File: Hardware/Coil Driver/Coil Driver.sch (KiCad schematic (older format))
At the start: 88 parts, among them J1 Barrel_Jack_Switch, J2 0.1\" Header, J3 Tag-connect-NL, J4 0.1\" Header, Q1 DMN3023L, Q2 DMN3023L, Q3 DMN3023L, Q4 DMN3023L, SW1 BTN_RST, SW2 BTN_USR1, SW3 BTN_USR2, U1 DGD05473, U2 MCP16331, U3 DGD05473, U4 STM32F070F6P6

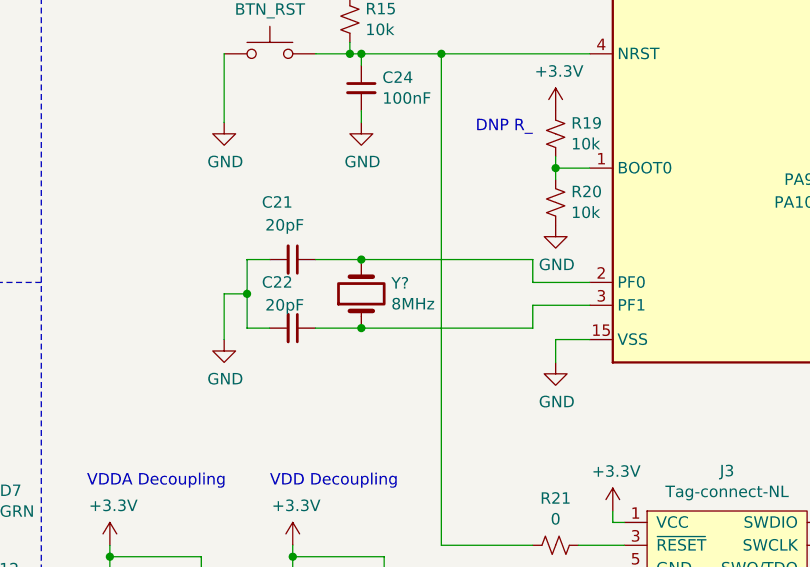
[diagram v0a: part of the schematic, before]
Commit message: completed first draft of part placement, and switching loop layout of gate drivers
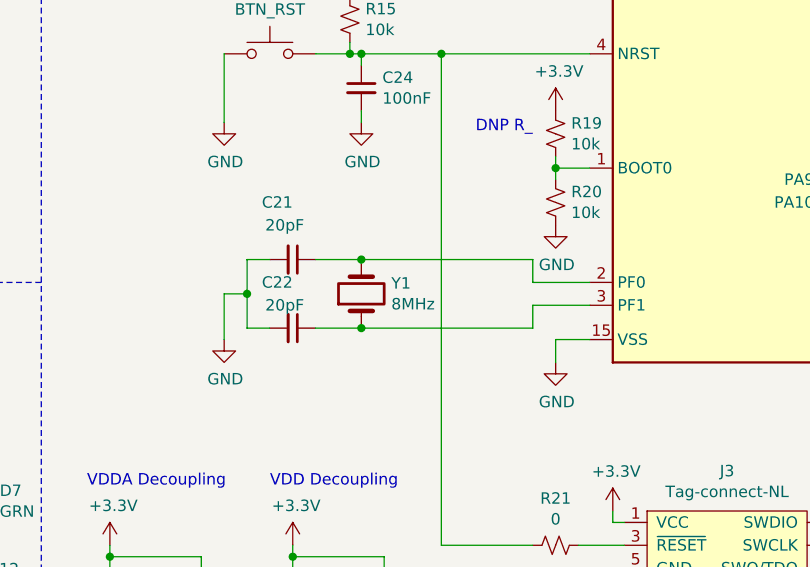
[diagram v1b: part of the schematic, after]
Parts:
- C6, C7, C8: footprint Capacitor_SMD:C_0603_1608Metric -> Capacitor_SMD:C_0402_1005Metric
- R18, R3: footprint Resistor_SMD:R_0603_1608Metric -> Resistor_SMD:R_0805_2012Metric
- Y1: renamed from Y?; footprint (none) -> Crystal:Crystal_SMD_5032-2Pin_5.0x3.2mm
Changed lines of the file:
@@
 F 0 "R3" V 2245 5100 50  0000 C CNN
 F 1 "10" V 2336 5100 50  0000 C CNN
-F 2 "Resistor_SMD:R_0603_1608Metric" H 2450 5100 50  0001 C CNN
+F 2 "Resistor_SMD:R_0805_2012Metric" H 2450 5100 50  0001 C CNN
 F 3 "~" H 2450 5100 50  0001 C CNN
 	1    2450 5100
@@
 F 0 "C8" V 2950 5150 50  0000 R CNN
 F 1 "100nF" V 2850 5200 50  0000 R CNN
-F 2 "Capacitor_SMD:C_0603_1608Metric" H 2750 5100 50  0001 C CNN
+F 2 "Capacitor_SMD:C_0402_1005Metric" H 2750 5100 50  0001 C CNN
 F 3 "~" H 2750 5100 50  0001 C CNN
 	1    2750 5100
@@
 F 0 "R18" V 6845 5100 50  0000 C CNN
 F 1 "10" V 6936 5100 50  0000 C CNN
-F 2 "Resistor_SMD:R_0603_1608Metric" H 7050 5100 50  0001 C CNN
+F 2 "Resistor_SMD:R_0805_2012Metric" H 7050 5100 50  0001 C CNN
 F 3 "~" H 7050 5100 50  0001 C CNN
 	1    7050 5100
@@
 F 0 "C7" H 2792 3246 50  0000 L CNN
 F 1 "100nF" H 2792 3155 50  0000 L CNN
-F 2 "Capacitor_SMD:C_0603_1608Metric" H 2700 3200 50  0001 C CNN
+F 2 "Capacitor_SMD:C_0402_1005Metric" H 2700 3200 50  0001 C CNN
 F 3 "~" H 2700 3200 50  0001 C CNN
 	1    2700 3200
@@
 F 0 "C6" H 2258 7146 50  0000 R CNN
 F 1 "100nF" H 2258 7055 50  0000 R CNN
-F 2 "Capacitor_SMD:C_0603_1608Metric" H 2350 7100 50  0001 C CNN
+F 2 "Capacitor_SMD:C_0402_1005Metric" H 2350 7100 50  0001 C CNN
 F 3 "~" H 2350 7100 50  0001 C CNN
 	1    2350 7100
@@
 	6200 2400 6400 2400
 $Comp
-L Device:Crystal Y?
+L Device:Crystal Y1
 U 1 1 60550A6D
 P 6400 2550
-F 0 "Y?" V 6446 2419 50  0000 R CNN
+F 0 "Y1" V 6446 2419 50  0000 R CNN
 F 1 "8MHz" V 6355 2419 50  0000 R CNN
-F 2 "" H 6400 2550 50  0001 C CNN
+F 2 "Crystal:Crystal_SMD_5032-2Pin_5.0x3.2mm" H 6400 2550 50  0001 C CNN
 F 3 "~" H 6400 2550 50  0001 C CNN
 	1    6400 2550

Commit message: Added internal layers, routed power input and buck converter, and repositioned a few components. Defined PCB shape and moved to center of drawing template.
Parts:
- L2: footprint Connector_PinHeader_2.54mm:PinHeader_1x02_P2.54mm_Vertical -> Connector_PinSocket_2.54mm:PinSocket_1x02_P2.54mm_Vertical
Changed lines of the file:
@@
 F 0 "L2" V 5100 5500 50  0000 C CNN
 F 1 "COIL" V 4950 5500 50  0000 C CNN
-F 2 "Connector_PinHeader_2.54mm:PinHeader_1x02_P2.54mm_Vertical" H 5000 5500 50  0001 C CNN
+F 2 "Connector_PinSocket_2.54mm:PinSocket_1x02_P2.54mm_Vertical" H 5000 5500 50  0001 C CNN
 F 3 "~" H 5000 5500 50  0001 C CNN
 	1    5000 5500

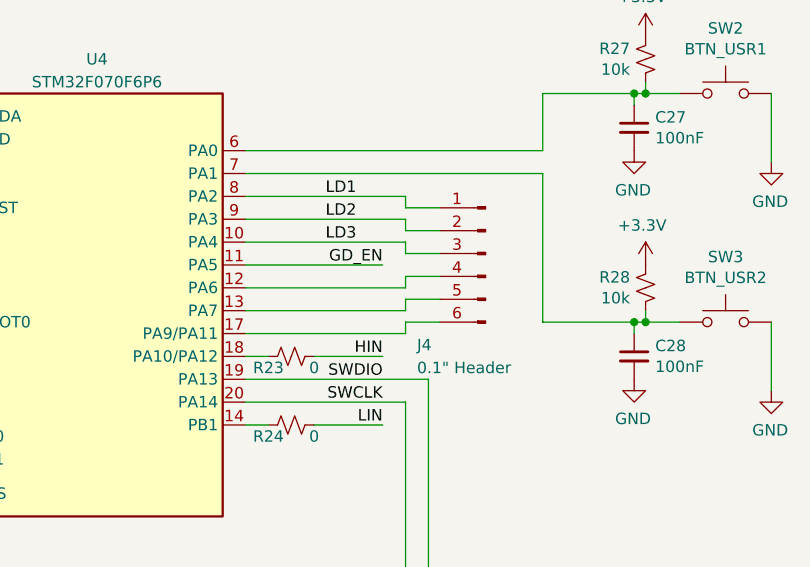
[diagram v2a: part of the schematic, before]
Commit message: Done with initial routing of microcontroller. Flipped order of extra IO exposed on header to ease routing. Added some power pours
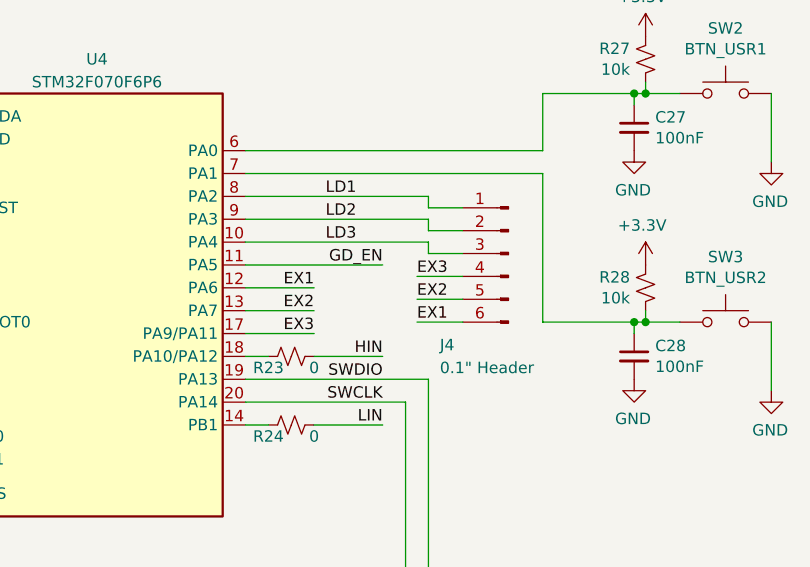
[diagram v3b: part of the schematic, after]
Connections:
- net EX1: now reaches U4.12 (PA6)
- net EX1: now also J4.6 (Pin_6); no longer J4.4 (Pin_4)
- net EX2: now reaches J4.5 (Pin_5), U4.13 (PA7)
- net EX3: now reaches U4.17 (PA9/PA11)
- net EX3: now also J4.4 (Pin_4); no longer J4.6 (Pin_6)
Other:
- moved on the sheet: J4
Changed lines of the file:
@@
 Wire Wire Line
 	10000 1350 10000 2000
-Text Label 9300 1750 2    50   ~ 0
-GD_EN
 Text Label 9300 2150 2    50   ~ 0
 HIN
@@
 L Connector:Conn_01x06_Male J4
 U 1 1 600594E3
-P 9750 1700
-F 0 "J4" H 10050 1300 50  0000 R CNN
-F 1 "0.1\" Header" H 10050 1200 50  0000 R CNN
-F 2 "Connector_PinHeader_2.54mm:PinHeader_1x06_P2.54mm_Vertical" H 9750 1700 50  0001 C CNN
-F 3 "~" H 9750 1700 50  0001 C CNN
-	1    9750 1700
-	-1   0    0    -1
-$EndComp
-Wire Wire Line
-	8700 1450 9400 1450
-Wire Wire Line
-	8700 2050 9400 2050
-Wire Wire Line
-	9400 2050 9400 2000
-Wire Wire Line
-	9400 2000 9550 2000
+P 9850 1700
+F 0 "J4" H 10150 1300 50  0000 R CNN
+F 1 "0.1\" Header" H 10150 1200 50  0000 R CNN
+F 2 "Connector_PinHeader_2.54mm:PinHeader_1x06_P2.54mm_Vertical" H 9850 1700 50  0001 C CNN
+F 3 "~" H 9850 1700 50  0001 C CNN
+	1    9850 1700
+	-1   0    0    -1
+$EndComp
 Wire Wire Line
 	9000 2150 9300 2150
@@
 $EndComp
 Wire Wire Line
-	8700 1950 9400 1950
-Wire Wire Line
-	9400 1950 9400 1900
-Wire Wire Line
-	9400 1900 9550 1900
-Wire Wire Line
-	9400 1850 9400 1800
-Wire Wire Line
-	9400 1800 9550 1800
-Wire Wire Line
-	8700 1850 9400 1850
-Wire Wire Line
-	9400 1650 9400 1700
-Wire Wire Line
-	9400 1700 9550 1700
-Wire Wire Line
-	8700 1650 9400 1650
-Wire Wire Line
-	9400 1550 9400 1600
-Wire Wire Line
-	9400 1600 9550 1600
-Wire Wire Line
-	8700 1550 9400 1550
-Wire Wire Line
-	9400 1450 9400 1500
-Wire Wire Line
-	9400 1500 9550 1500
+	9500 1650 9500 1700
+Wire Wire Line
+	9500 1700 9650 1700
+Wire Wire Line
+	9500 1550 9500 1600
+Wire Wire Line
+	9500 1600 9650 1600
+Wire Wire Line
+	9500 1450 9500 1500
+Wire Wire Line
+	9500 1500 9650 1500
 $Comp
 L Device:C_Small C20
@@
 	0    1    1    0
 $EndComp
-Text Label 9050 1450 0    50   ~ 0
-LD1
-Text Label 9050 1550 0    50   ~ 0
-LD2
-Text Label 9050 1650 0    50   ~ 0
-LD3
 $Comp
 L Device:LED D10
@@
 Wire Wire Line
 	6400 2400 7150 2400
+Wire Wire Line
+	8700 1850 9000 1850
+Wire Wire Line
+	8700 1950 9000 1950
+Wire Wire Line
+	8700 2050 9000 2050
+Text Label 9000 1850 2    50   ~ 0
+EX1
+Text Label 9000 1950 2    50   ~ 0
+EX2
+Text Label 9000 2050 2    50   ~ 0
+EX3
+Text Label 9450 2000 0    50   ~ 0
+EX1
+Text Label 9450 1900 0    50   ~ 0
+EX2
+Text Label 9450 1800 0    50   ~ 0
+EX3
+Wire Wire Line
+	9650 1800 9450 1800
+Wire Wire Line
+	9450 1900 9650 1900
+Wire Wire Line
+	9650 2000 9450 2000
+Wire Wire Line
+	8700 1450 9500 1450
+Wire Wire Line
+	8700 1550 9500 1550
+Wire Wire Line
+	8700 1650 9500 1650
+Text Label 9300 1750 2    50   ~ 0
+GD_EN
+Text Label 9050 1650 0    50   ~ 0
+LD3
+Text Label 9050 1550 0    50   ~ 0
+LD2
+Text Label 9050 1450 0    50   ~ 0
+LD1
 $EndSCHEMATC

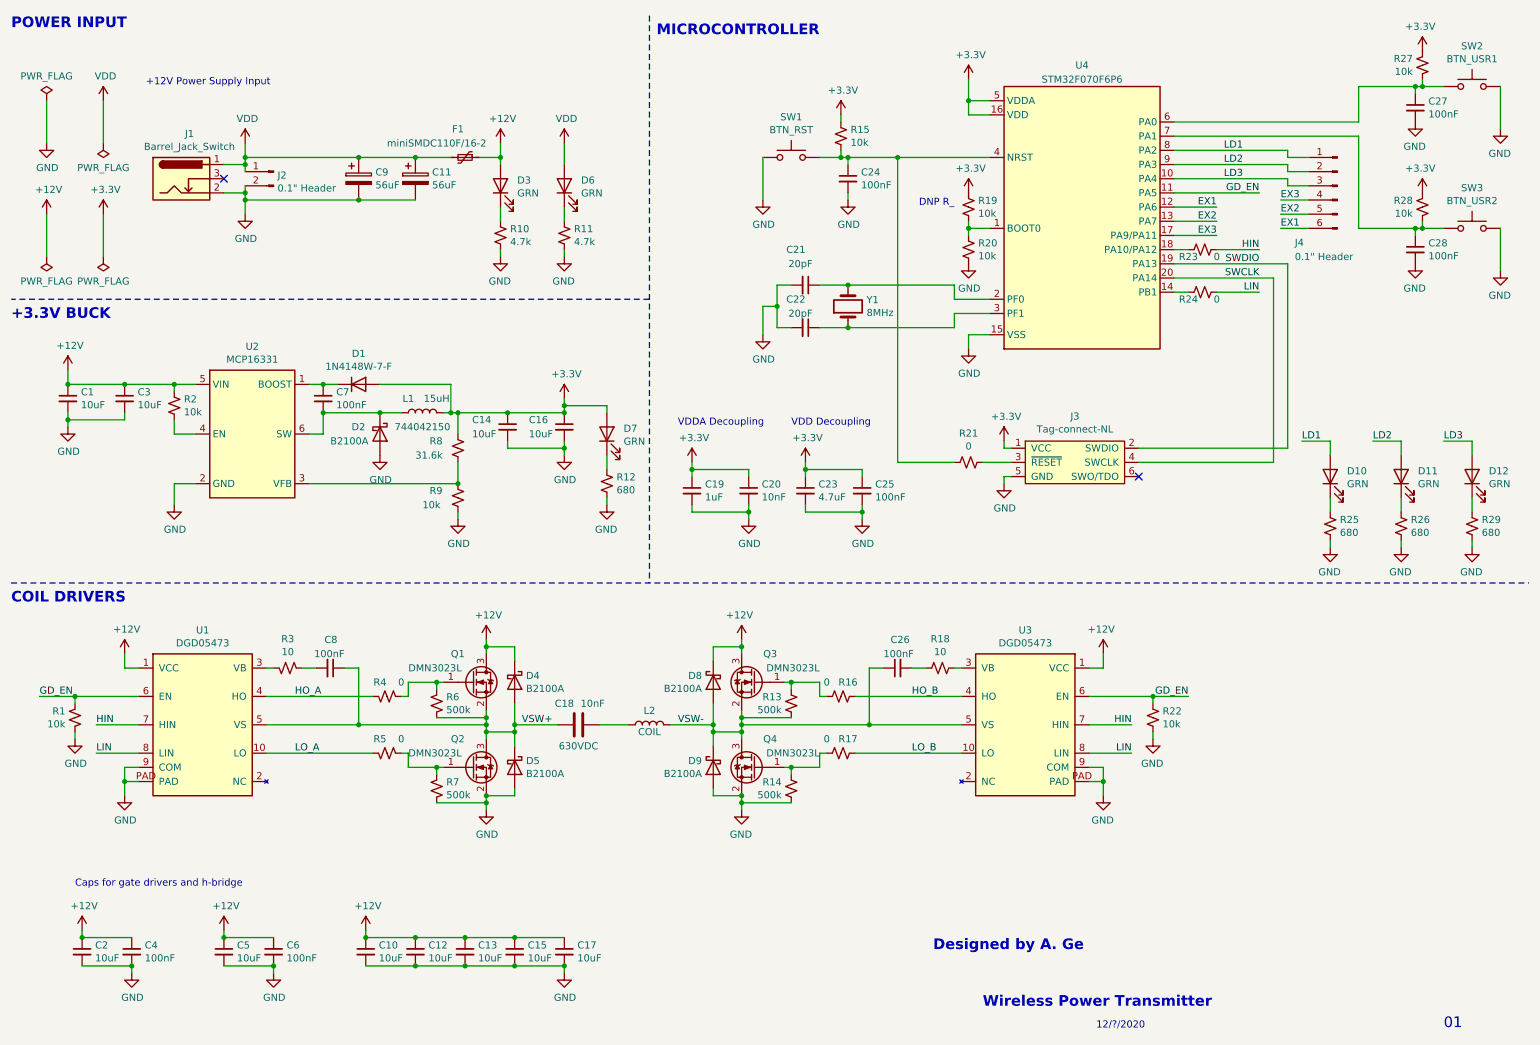
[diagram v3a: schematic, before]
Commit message: Positioned all designators and added logo library
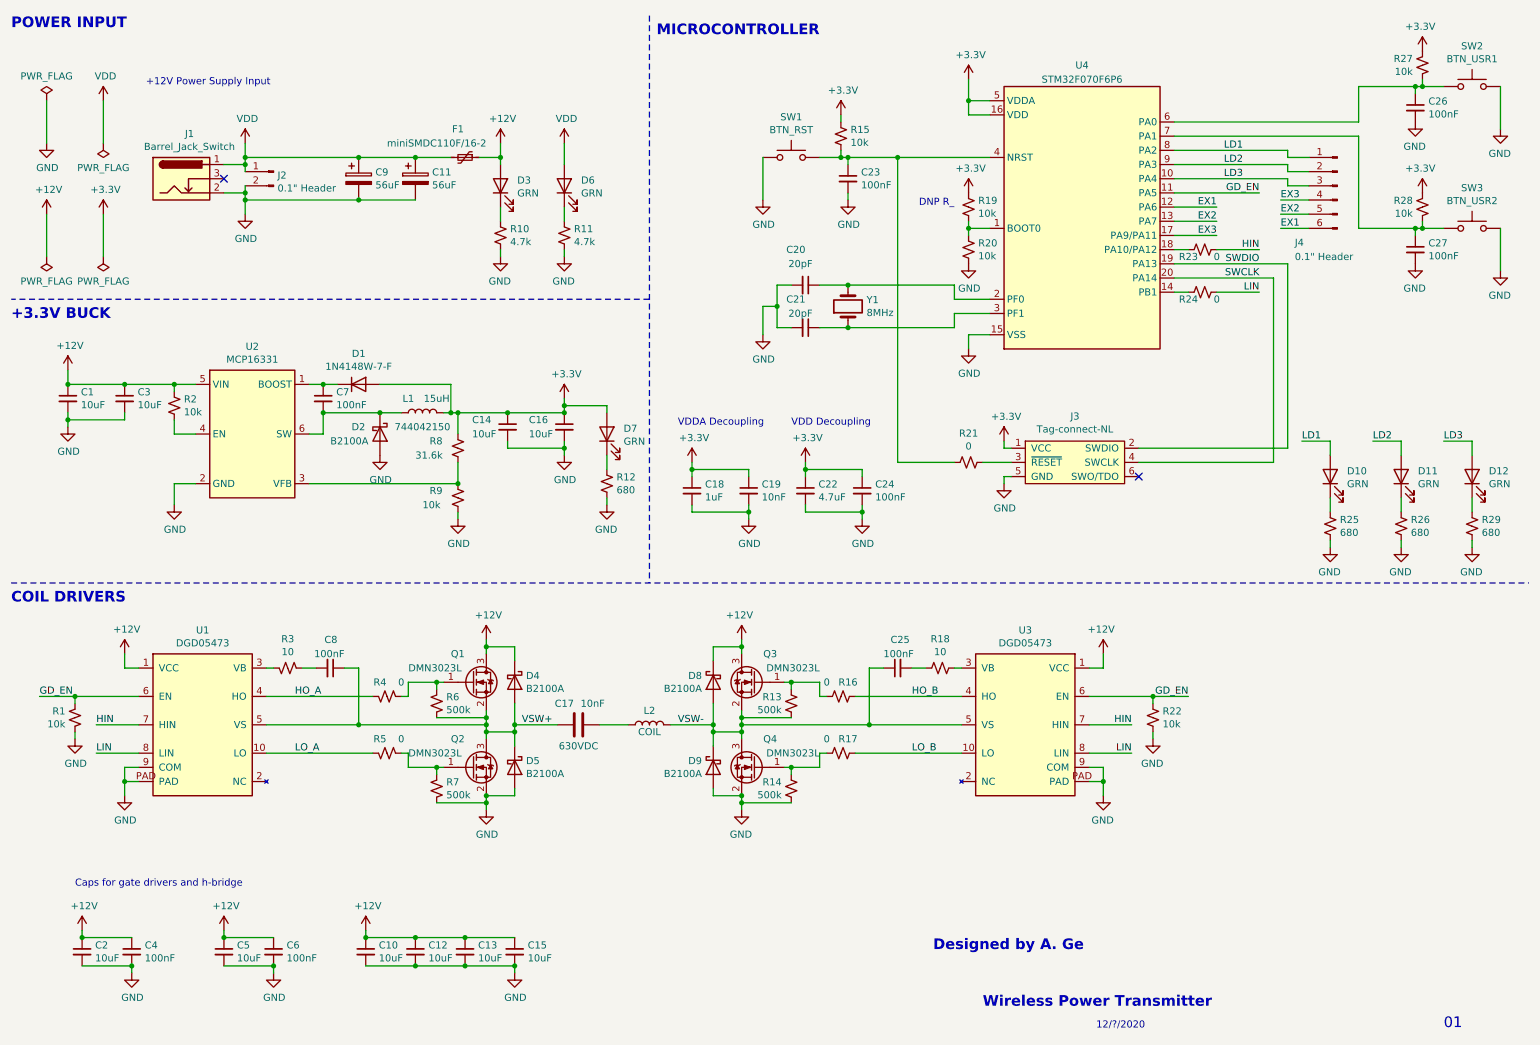
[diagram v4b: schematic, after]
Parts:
- removed C17: 10uF, Capacitor_SMD:C_0603_1608Metric, symbol Device:C_Small
- renumbered C18 to C17, C19 to C18, C20 to C19, C21 to C20, C22 to C21, C23 to C22, C24 to C23, C25 to C24, C26 to C25, C27 to C26, C28 to C27

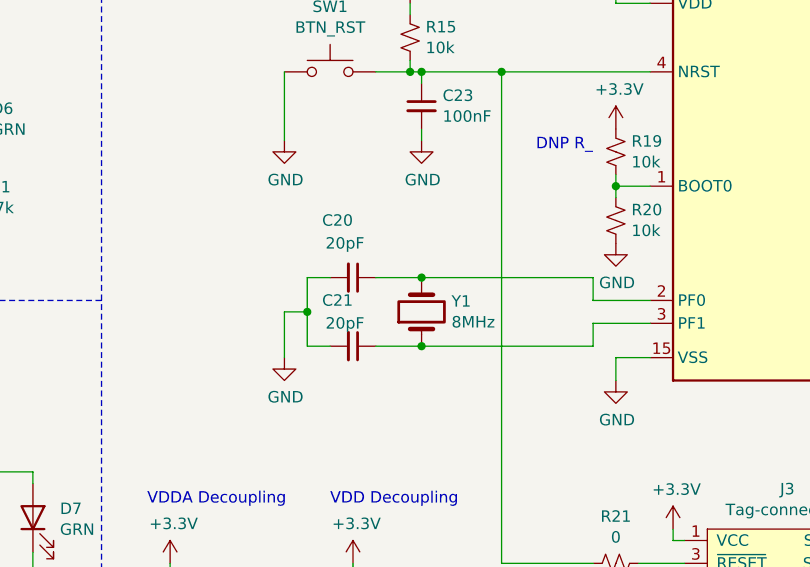
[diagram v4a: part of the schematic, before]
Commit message: committing final changes to coil driver, and creating new kicad folder for receiver
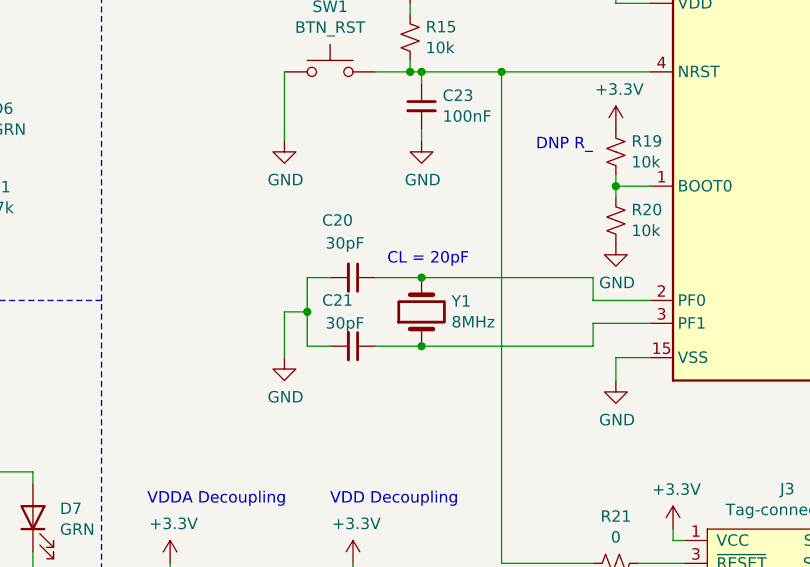
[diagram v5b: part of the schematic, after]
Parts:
- C20, C21: value 20pF -> 30pF
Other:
- note added: "CL = 20pF\n"
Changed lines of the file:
@@
 P 6100 2700
 F 0 "C21" V 6300 2700 50  0000 R CNN
-F 1 "20pF" V 6200 2750 50  0000 R CNN
+F 1 "30pF" V 6200 2750 50  0000 R CNN
 F 2 "Capacitor_SMD:C_0402_1005Metric" H 6100 2700 50  0001 C CNN
 F 3 "~" H 6100 2700 50  0001 C CNN
@@
 P 6100 2400
 F 0 "C20" V 6350 2400 50  0000 R CNN
-F 1 "20pF" V 6250 2450 50  0000 R CNN
+F 1 "30pF" V 6250 2450 50  0000 R CNN
 F 2 "Capacitor_SMD:C_0402_1005Metric" H 6100 2400 50  0001 C CNN
 F 3 "~" H 6100 2400 50  0001 C CNN
@@
 Text Notes 500  4650 0    75   ~ 15
 COIL DRIVERS
-Wire Notes Line
-	500  4500 11200 4500
 $Comp
 L power:GND #PWR043
@@
 	4050 7200 4050 7250
 Connection ~ 4050 7200
+Wire Notes Line
+	500  4500 11200 4500
+Text Notes 6250 2350 0    50   ~ 0
+CL = 20pF\n
 $EndSCHEMATC

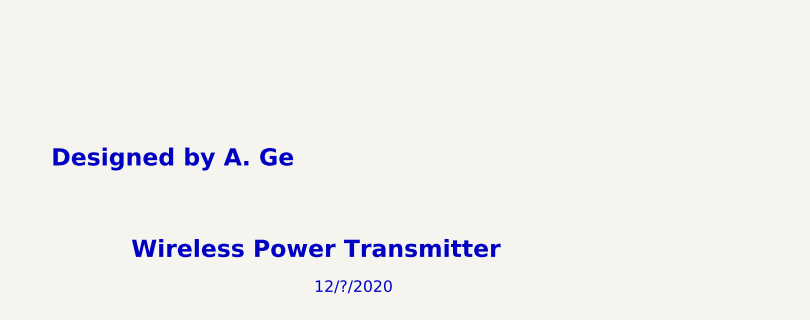
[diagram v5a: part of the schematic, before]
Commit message: updated title block parameters for both schematic. In receiver, modified symbol of STM32, added to schematic and also added crystal, decoupling caps, and buttons
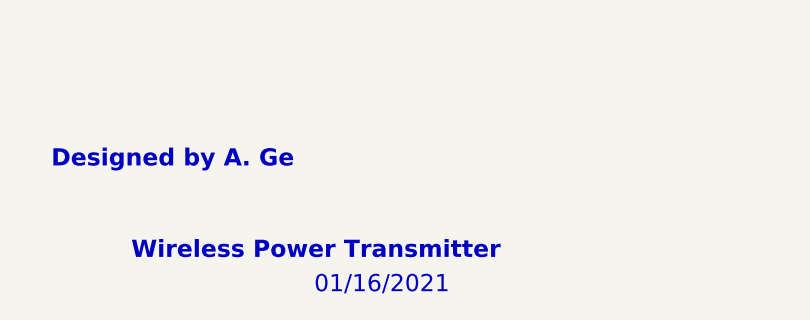
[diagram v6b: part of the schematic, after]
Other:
- note added: "01/16/2021"
- note removed: "12/?/2020"
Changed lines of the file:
@@
 Text Notes 7350 7500 0    75   ~ 15
 Wireless Power Transmitter
-Text Notes 8150 7650 0    50   ~ 0
-12/?/2020
+Text Notes 8150 7650 0    75   ~ 0
+01/16/2021
 Text Notes 10600 7650 0    75   ~ 0
 01

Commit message: Added an MPN to electrolytic caps in coil driver. Added debug LEDs to 3 pins on receiver micro
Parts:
- C11, C9: MPN (none) -> 865080443008
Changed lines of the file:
@@
 F 2 "Capacitor_SMD:CP_Elec_6.3x7.7" H 2988 1500 50  0001 C CNN
 F 3 "~" H 2950 1650 50  0001 C CNN
+F 4 "865080443008" H 2950 1650 50  0001 C CNN "MPN"
 	1    2950 1650
 	1    0    0    -1
@@
 F 2 "Capacitor_SMD:CP_Elec_6.3x7.7" H 3388 1500 50  0001 C CNN
 F 3 "~" H 3350 1650 50  0001 C CNN
+F 4 "865080443008" H 3350 1650 50  0001 C CNN "MPN"
 	1    3350 1650
 	1    0    0    -1
